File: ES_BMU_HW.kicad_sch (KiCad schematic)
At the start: 18 parts, among them J1 Conn_02x02_Top_Bottom, J2 Conn_02x02_Top_Bottom, J3 Conn_02x03_Top_Bottom, J4 Conn_02x06_Top_Bottom, J6 Conn_02x04_Top_Bottom, U1 TPS542025, U7 TLV777

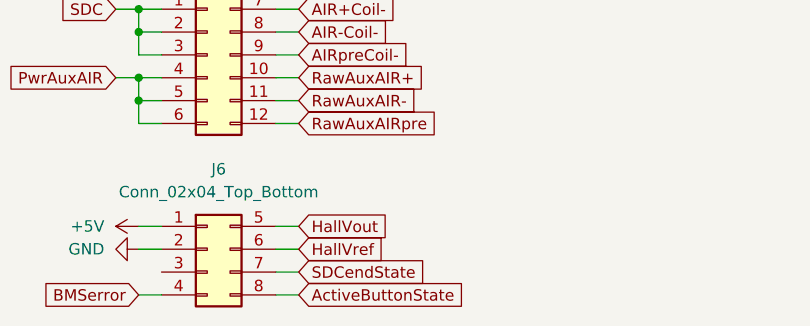
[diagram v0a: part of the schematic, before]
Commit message: Fusibles eliminats de la mesura dels contactors auxiliars Canvi de lloc dels enables del CAN Emplaçament dels inputs, CAN i LEDs al Layout
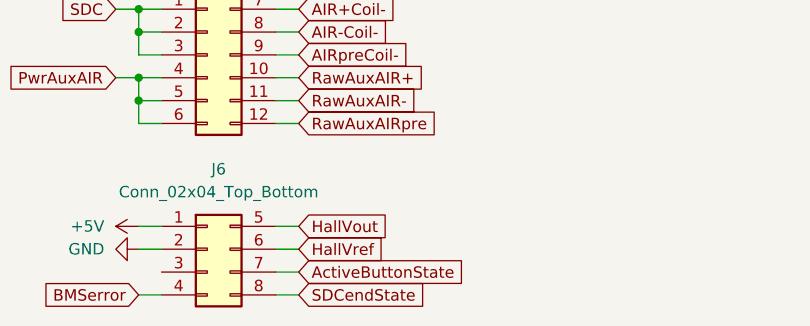
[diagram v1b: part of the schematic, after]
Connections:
- net ActiveButtonState: now also J6.7 (Pin_7); no longer J6.8 (Pin_8)
- net SDCendState: now also J6.8 (Pin_8); no longer J6.7 (Pin_7)
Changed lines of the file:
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@@
 	(global_label "SDCendState"
 		(shape input)
+		(at 57.15 184.15 0)
+		(fields_autoplaced yes)
+		(effects
+			(font
+				(size 1.27 1.27)
+			)
+			(justify left)
+		)
+		(property "Intersheetrefs" "${INTERSHEET_REFS}"
+			(at 76.766 184.15 0)
+			(effects
+				(font
+					(size 1.27 1.27)
+				)
+				(justify left)
+				(hide yes)
+			)
+		)
+	)
+	(global_label "CAN2L"
+		(shape input)
+		(at 57.15 142.24 0)
+		(fields_autoplaced yes)
+		(effects
+			(font
+				(size 1.27 1.27)
+			)
+			(justify left)
+		)
+		(property "Intersheetrefs" "${INTERSHEET_REFS}"
+			(at 66.0619 142.24 0)
+			(effects
+				(font
+					(size 1.27 1.27)
+				)
+				(justify left)
+				(hide yes)
+			)
+		)
+	)
+	(global_label "CAN1L"
+		(shape input)
+		(at 57.15 137.16 0)
+		(fields_autoplaced yes)
+		(effects
+			(font
+				(size 1.27 1.27)
+			)
+			(justify left)
+		)
+		(property "Intersheetrefs" "${INTERSHEET_REFS}"
+			(at 66.0619 137.16 0)
+			(effects
+				(font
+					(size 1.27 1.27)
+				)
+				(justify left)
+				(hide yes)
+			)
+		)
+	)
+	(global_label "HallVout"
+		(shape input)
+		(at 57.15 176.53 0)
+		(fields_autoplaced yes)
+		(effects
+			(font
+				(size 1.27 1.27)
+			)
+			(justify left)
+		)
+		(property "Intersheetrefs" "${INTERSHEET_REFS}"
+			(at 68.0574 176.53 0)
+			(effects
+				(font
+					(size 1.27 1.27)
+				)
+				(justify left)
+				(hide yes)
+			)
+		)
+	)
+	(global_label "CAN1H"
+		(shape input)
+		(at 39.37 137.16 180)
+		(fields_autoplaced yes)
+		(effects
+			(font
+				(size 1.27 1.27)
+			)
+			(justify right)
+		)
+		(property "Intersheetrefs" "${INTERSHEET_REFS}"
+			(at 30.1557 137.16 0)
+			(effects
+				(font
+					(size 1.27 1.27)
+				)
+				(justify right)
+				(hide yes)
+			)
+		)
+	)
+	(global_label "BMSerror"
+		(shape input)
+		(at 39.37 184.15 180)
+		(fields_autoplaced yes)
+		(effects
+			(font
+				(size 1.27 1.27)
+			)
+			(justify right)
+		)
+		(property "Intersheetrefs" "${INTERSHEET_REFS}"
+			(at 27.8577 184.15 0)
+			(effects
+				(font
+					(size 1.27 1.27)
+				)
+				(justify right)
+				(hide yes)
+			)
+		)
+	)
+	(global_label "CAN1L"
+		(shape input)
+		(at 57.15 139.7 0)
+		(fields_autoplaced yes)
+		(effects
+			(font
+				(size 1.27 1.27)
+			)
+			(justify left)
+		)
+		(property "Intersheetrefs" "${INTERSHEET_REFS}"
+			(at 66.0619 139.7 0)
+			(effects
+				(font
+					(size 1.27 1.27)
+				)
+				(justify left)
+				(hide yes)
+			)
+		)
+	)
+	(global_label "AIR+Coil-"
+		(shape input)
+		(at 57.15 152.4 0)
+		(fields_autoplaced yes)
+		(effects
+			(font
+				(size 1.27 1.27)
+			)
+			(justify left)
+		)
+		(property "Intersheetrefs" "${INTERSHEET_REFS}"
+			(at 69.9324 152.4 0)
+			(effects
+				(font
+					(size 1.27 1.27)
+				)
+				(justify left)
+				(hide yes)
+			)
+		)
+	)
+	(global_label "isoIMA"
+		(shape input)
+		(at 57.15 111.76 0)
+		(fields_autoplaced yes)
+		(effects
+			(font
+				(size 1.27 1.27)
+			)
+			(justify left)
+		)
+		(property "Intersheetrefs" "${INTERSHEET_REFS}"
+			(at 66.0619 111.76 0)
+			(effects
+				(font
+					(size 1.27 1.27)
+				)
+				(justify left)
+				(hide yes)
+			)
+		)
+	)
+	(global_label "HallVref"
+		(shape input)
+		(at 57.15 179.07 0)
+		(fields_autoplaced yes)
+		(effects
+			(font
+				(size 1.27 1.27)
+			)
+			(justify left)
+		)
+		(property "Intersheetrefs" "${INTERSHEET_REFS}"
+			(at 67.6342 179.07 0)
+			(effects
+				(font
+					(size 1.27 1.27)
+				)
+				(justify left)
+				(hide yes)
+			)
+		)
+	)
+	(global_label "ActiveButtonState"
+		(shape input)
 		(at 57.15 181.61 0)
 		(fields_autoplaced yes)
@@
 			(effects
 				(font
-					(size 1.27 1.27)
-				)
-				(justify left)
-				(hide yes)
-			)
-		)
-	)
-	(global_label "CAN2L"
-		(shape input)
-		(at 57.15 142.24 0)
-		(fields_autoplaced yes)
-		(effects
-			(font
-				(size 1.27 1.27)
-			)
-			(justify left)
-		)
-		(property "Intersheetrefs" "${INTERSHEET_REFS}"
-			(at 66.0619 142.24 0)
-			(effects
-				(font
-					(size 1.27 1.27)
-				)
-				(justify left)
-				(hide yes)
-			)
-		)
-	)
-	(global_label "CAN1L"
-		(shape input)
-		(at 57.15 137.16 0)
-		(fields_autoplaced yes)
-		(effects
-			(font
-				(size 1.27 1.27)
-			)
-			(justify left)
-		)
-		(property "Intersheetrefs" "${INTERSHEET_REFS}"
-			(at 66.0619 137.16 0)
-			(effects
-				(font
-					(size 1.27 1.27)
-				)
-				(justify left)
-				(hide yes)
-			)
-		)
-	)
-	(global_label "HallVout"
-		(shape input)
-		(at 57.15 176.53 0)
-		(fields_autoplaced yes)
-		(effects
-			(font
-				(size 1.27 1.27)
-			)
-			(justify left)
-		)
-		(property "Intersheetrefs" "${INTERSHEET_REFS}"
-			(at 68.0574 176.53 0)
-			(effects
-				(font
-					(size 1.27 1.27)
-				)
-				(justify left)
-				(hide yes)
-			)
-		)
-	)
-	(global_label "CAN1H"
-		(shape input)
-		(at 39.37 137.16 180)
-		(fields_autoplaced yes)
-		(effects
-			(font
-				(size 1.27 1.27)
-			)
-			(justify right)
-		)
-		(property "Intersheetrefs" "${INTERSHEET_REFS}"
-			(at 30.1557 137.16 0)
-			(effects
-				(font
-					(size 1.27 1.27)
-				)
-				(justify right)
-				(hide yes)
-			)
-		)
-	)
-	(global_label "BMSerror"
-		(shape input)
-		(at 39.37 184.15 180)
-		(fields_autoplaced yes)
-		(effects
-			(font
-				(size 1.27 1.27)
-			)
-			(justify right)
-		)
-		(property "Intersheetrefs" "${INTERSHEET_REFS}"
-			(at 27.8577 184.15 0)
-			(effects
-				(font
-					(size 1.27 1.27)
-				)
-				(justify right)
-				(hide yes)
-			)
-		)
-	)
-	(global_label "CAN1L"
-		(shape input)
-		(at 57.15 139.7 0)
-		(fields_autoplaced yes)
-		(effects
-			(font
-				(size 1.27 1.27)
-			)
-			(justify left)
-		)
-		(property "Intersheetrefs" "${INTERSHEET_REFS}"
-			(at 66.0619 139.7 0)
-			(effects
-				(font
-					(size 1.27 1.27)
-				)
-				(justify left)
-				(hide yes)
-			)
-		)
-	)
-	(global_label "AIR+Coil-"
-		(shape input)
-		(at 57.15 152.4 0)
-		(fields_autoplaced yes)
-		(effects
-			(font
-				(size 1.27 1.27)
-			)
-			(justify left)
-		)
-		(property "Intersheetrefs" "${INTERSHEET_REFS}"
-			(at 69.9324 152.4 0)
-			(effects
-				(font
-					(size 1.27 1.27)
-				)
-				(justify left)
-				(hide yes)
-			)
-		)
-	)
-	(global_label "isoIMA"
-		(shape input)
-		(at 57.15 111.76 0)
-		(fields_autoplaced yes)
-		(effects
-			(font
-				(size 1.27 1.27)
-			)
-			(justify left)
-		)
-		(property "Intersheetrefs" "${INTERSHEET_REFS}"
-			(at 66.0619 111.76 0)
-			(effects
-				(font
-					(size 1.27 1.27)
-				)
-				(justify left)
-				(hide yes)
-			)
-		)
-	)
-	(global_label "HallVref"
-		(shape input)
-		(at 57.15 179.07 0)
-		(fields_autoplaced yes)
-		(effects
-			(font
-				(size 1.27 1.27)
-			)
-			(justify left)
-		)
-		(property "Intersheetrefs" "${INTERSHEET_REFS}"
-			(at 67.6342 179.07 0)
-			(effects
-				(font
-					(size 1.27 1.27)
-				)
-				(justify left)
-				(hide yes)
-			)
-		)
-	)
-	(global_label "ActiveButtonState"
-		(shape input)
-		(at 57.15 184.15 0)
-		(fields_autoplaced yes)
-		(effects
-			(font
-				(size 1.27 1.27)
-			)
-			(justify left)
-		)
-		(property "Intersheetrefs" "${INTERSHEET_REFS}"
-			(at 76.766 184.15 0)
-			(effects
-				(font

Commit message: Layout avançat amb el placement acabat
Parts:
- added H1, H2, H3, H4: MountingHole_Pad, MountingHole:MountingHole_3.5mm, symbol Mechanical:MountingHole
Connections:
- net AIR+Coil-: now also J4.1 (Pin_1); no longer J4.7 (Pin_7)
- net AIR-Coil-: now also J4.2 (Pin_2); no longer J4.8 (Pin_8)
- net AIRpreCoil-: now also J4.3 (Pin_3); no longer J4.9 (Pin_9)
- net GND: now also J2.1 (Pin_1); no longer J2.4 (Pin_4)
- net PwrAuxAIR: now also J4.10 (Pin_10), J4.11 (Pin_11), J4.12 (Pin_12); no longer J4.4 (Pin_4), J4.5 (Pin_5), J4.6 (Pin_6)
- net RawAuxAIR+: now also J4.6 (Pin_6); no longer J4.10 (Pin_10)
- net RawAuxAIR-: now also J4.5 (Pin_5); no longer J4.11 (Pin_11)
- net RawAuxAIRpre: now also J4.4 (Pin_4); no longer J4.12 (Pin_12)
- net SDC: now also J4.7 (Pin_7), J4.8 (Pin_8), J4.9 (Pin_9); no longer J4.1 (Pin_1), J4.2 (Pin_2), J4.3 (Pin_3)
- net isoIMA: now also J1.4 (Pin_4); no longer J1.3 (Pin_3)
- net isoIPA: now also J1.3 (Pin_3); no longer J1.1 (Pin_1)
- net ActiveButtonState renamed ActiveButton
- net BMSerror renamed BMSerrorOutput
- net SDCendState renamed SDCinput

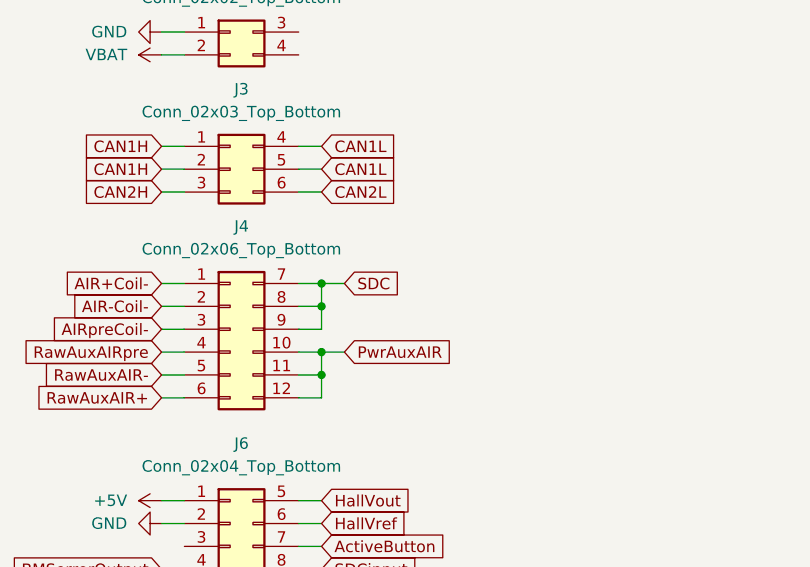
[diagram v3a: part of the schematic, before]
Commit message: Layout acabat amb components, pistes i serigrafia completa
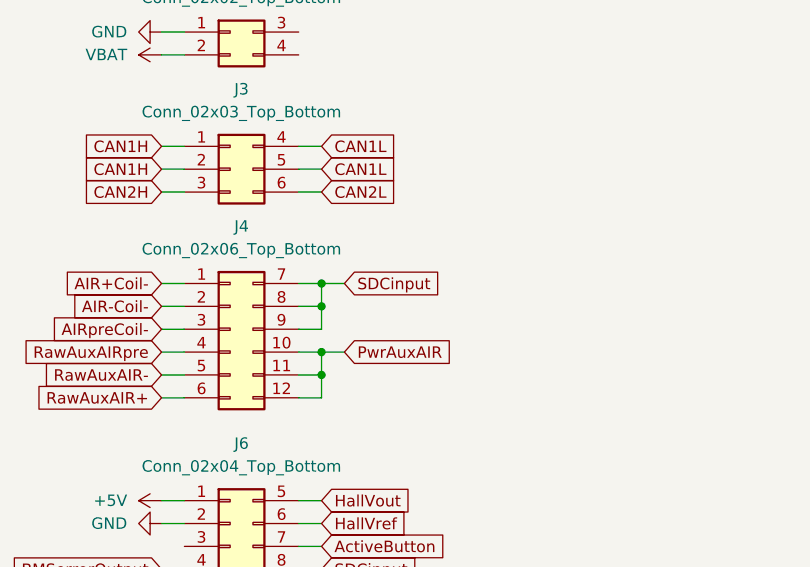
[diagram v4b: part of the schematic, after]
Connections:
- net SDC is gone; now on net SDCinput: J4.7 (Pin_7), J4.8 (Pin_8), J4.9 (Pin_9)
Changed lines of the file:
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@@
-		)
-	)
-	(global_label "SDC"
-		(shape input)
-		(at 59.69 152.4 0)
-		(fields_autoplaced yes)
-		(effects
-			(font
-				(size 1.27 1.27)
-			)
-			(justify left)
-		)
-		(property "Intersheetrefs" "${INTERSHEET_REFS}"
-			(at 66.4247 152.4 0)
-			(hide yes)
-			(show_name no)
-			(do_not_autoplace no)
-			(effects
-				(font
-					(size 1.27 1.27)
-				)
-				(justify left)
-			)
 		)
 	)
@@
 			(hide yes)
 			(show_name no)
+			(do_not_autoplace no)
+			(effects
+				(font
+					(size 1.27 1.27)
+				)
+				(justify left)
+			)
+		)
+	)
+	(global_label "SDCinput"
+		(shape input)
+		(at 59.69 152.4 0)
+		(fields_autoplaced yes)
+		(effects
+			(font
+				(size 1.27 1.27)
+			)
+			(justify left)
+		)
+		(property "Intersheetrefs" "${INTERSHEET_REFS}"
+			(at 71.2022 152.4 0)
+			(hide yes)
+			(show_name no)

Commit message: updated schematics template
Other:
- note added: "BMU"
- note added: "CAN COMMUNICATIONS"
- note added: "Changelog"
- note added: "MOUNTING HOLES"
- note added: "PINOUT CONFIGURATION"
- note added: "POWER RELAYS GPIO"
- note added: "POWER SUPPLY"
- note added: "POWER SUPPLY CONDITIONING CIRCUIT"
- note added: "SENSORS & SIGNALS"
- note added: "isoSPI COMMUNICATIONS"
- note added: "v1.0"
- company: (none) -> EUSS Motorsport
- title: (none) -> BMU
- moved on the sheet: C1, C2, C3, C4, C5, C6, C7, C8, D1, F1, H1, H2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
